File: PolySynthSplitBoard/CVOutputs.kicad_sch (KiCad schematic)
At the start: 121 parts, among them U301 DAC7578xPW, U302 TL074, U303 TL072, U304 TL074, U305 TL072, U306 TMUX4051, U307 TL074, U308 TMUX4051, U309 TL072, U310 TL074, U311 TL072, U312 TL074, U313 TMUX4051, U314 TMUX4051, U315 TL074, U316 TL074, U317 TL074, U318 TL072, U319 TL072, U320 TL072, U321 TMUX4051, U322 TMUX4051, U323 TMUX4051

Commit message: lower board
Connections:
- net FOLD_DAC: now also U301.11 (VOUTF); no longer U301.6 (VOUTE)
- net PWM1_DAC: now also U301.6 (VOUTE); no longer U301.5 (VOUTC)
- net PWM2_DAC: now also U301.5 (VOUTC); no longer U301.12 (VOUTD)
- net VCA_DAC: now also U301.12 (VOUTD); no longer U301.11 (VOUTF)
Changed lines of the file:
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@@
 	(wire
 		(pts
-			(xy 76.2 71.628) (xy 79.756 71.628)
+			(xy 76.2 71.628) (xy 80.518 71.628)
 		)
 		(stroke
@@
 	(wire
 		(pts
+			(xy 76.2 69.088) (xy 80.518 69.088)
+		)
+		(stroke
+			(width 0)
+			(type default)
+		)
+	)
+	(wire
+		(pts
 			(xy 432.816 125.984) (xy 432.816 117.094)
 		)
@@
 	(wire
 		(pts
-			(xy 76.2 69.088) (xy 79.756 69.088)
-		)
-		(stroke
-			(width 0)
-			(type default)
-		)
-	)
-	(wire
-		(pts
 			(xy 495.808 176.276) (xy 500.888 176.276)
 		)
@@
 	(global_label "PWM2_DAC"
 		(shape output)
-		(at 79.756 71.628 0)
+		(at 80.518 69.088 0)
 		(fields_autoplaced yes)
 		(effects
@@
 		)
 		(property "Intersheetrefs" "${INTERSHEET_REFS}"
-			(at 92.7197 71.628 0)
+			(at 93.4817 69.088 0)
 			(effects
 				(font
@@
 	(global_label "VCA_DAC"
 		(shape output)
-		(at 80.518 76.708 0)
+		(at 80.518 71.628 0)
 		(fields_autoplaced yes)
 		(effects
@@
 		)
 		(property "Intersheetrefs" "${INTERSHEET_REFS}"
-			(at 91.5466 76.708 0)
+			(at 91.5466 71.628 0)
 			(effects
 				(font
@@
 	(global_label "PWM1_DAC"
 		(shape output)
-		(at 79.756 69.088 0)
+		(at 80.518 74.168 0)
 		(fields_autoplaced yes)
 		(effects
@@
 		)
 		(property "Intersheetrefs" "${INTERSHEET_REFS}"
-			(at 92.7197 69.088 0)
+			(at 93.4817 74.168 0)
 			(effects
 				(font
@@
 	(global_label "FOLD_DAC"
 		(shape output)
-		(at 80.518 74.168 0)
+		(at 80.518 76.708 0)
 		(fields_autoplaced yes)
 		(effects
@@
 		)
 		(property "Intersheetrefs" "${INTERSHEET_REFS}"
-			(at 92.8166 74.168 0)
+			(at 92.8166 76.708 0)
 			(effects
 				(font

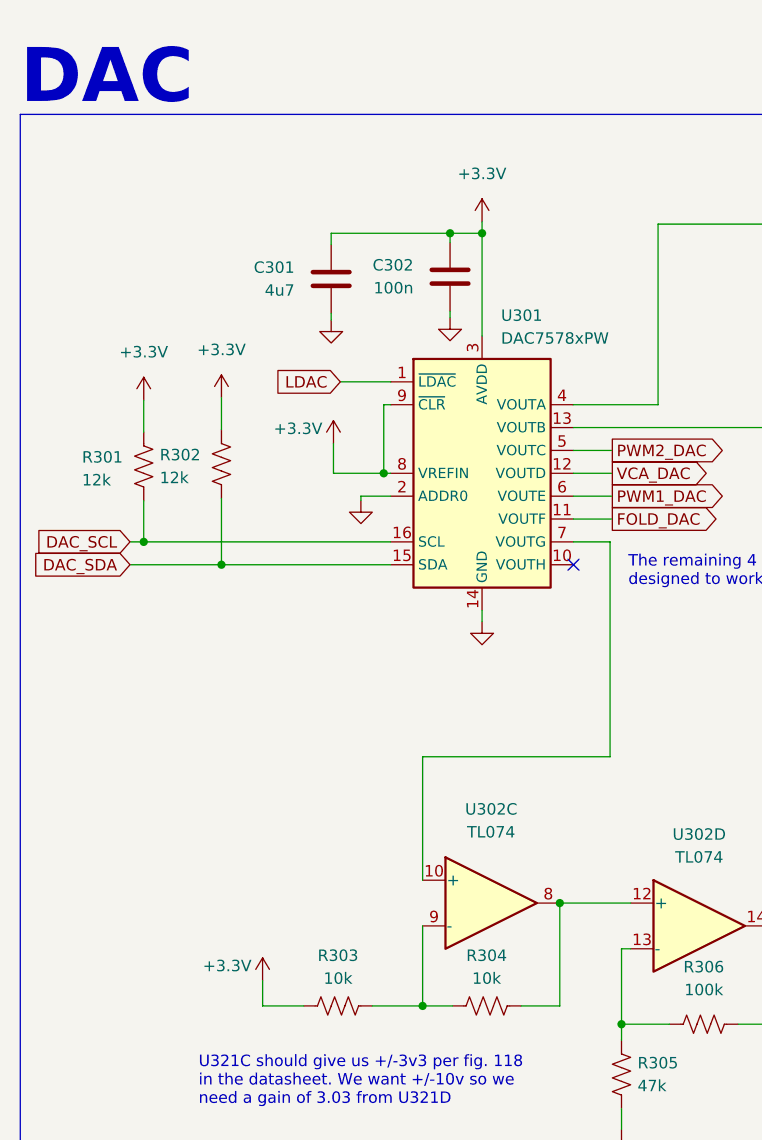
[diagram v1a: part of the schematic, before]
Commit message: removed copper pour
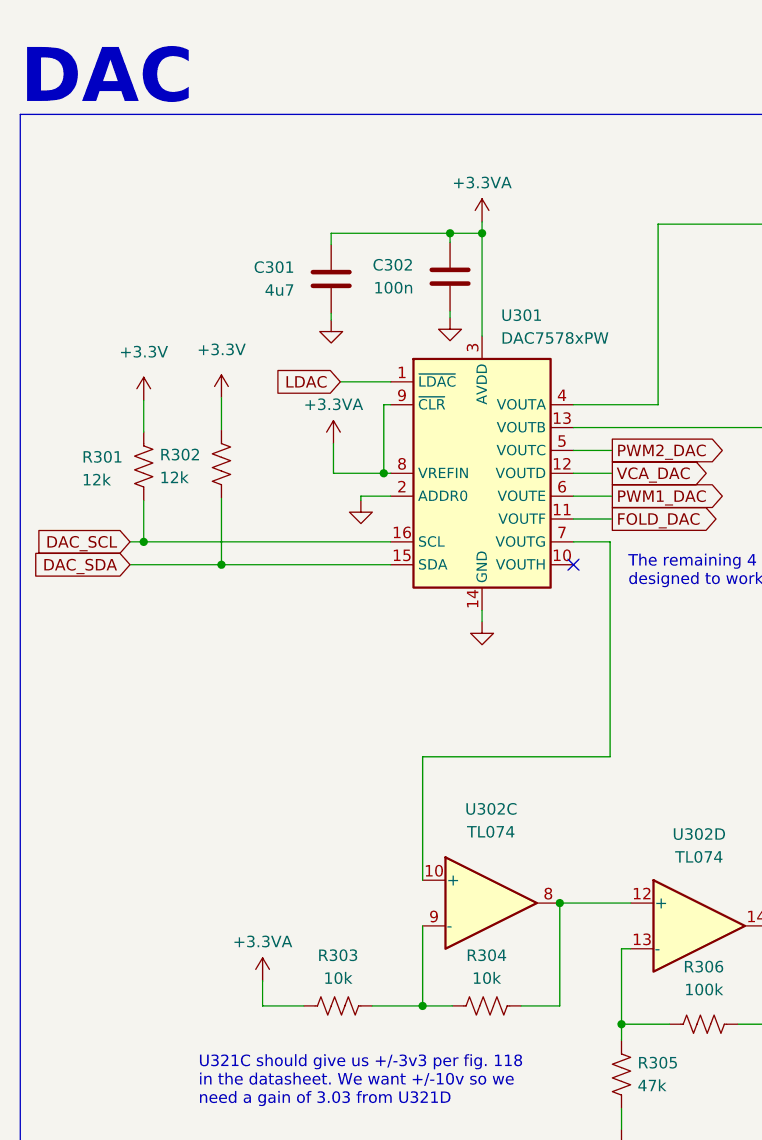
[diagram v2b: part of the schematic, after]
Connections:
- net +3.3V: no longer C301.1, C302.1, R303.1, U301.3 (AVDD), U301.8 (VREFIN), U301.9 (~{CLR})
- new net +3.3VA: C301.1, C302.1, R303.1, U301.3 (AVDD), U301.8 (VREFIN), U301.9 (~{CLR})
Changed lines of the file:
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@@
 	)
 	(symbol
-		(lib_name "+3.3V_1")
-		(lib_id "power:+3.3V")
-		(at 66.04 43.688 0)
-		(unit 1)
-		(exclude_from_sim no)
-		(in_bom yes)
-		(on_board yes)
-		(dnp no)
-		(fields_autoplaced yes)
-		(property "Reference" "#PWR0308"
-			(at 66.04 47.498 0)
-			(effects
-				(font
-					(size 1.27 1.27)
-				)
-				(hide yes)
-			)
-		)
-		(property "Value" "+3.3V"
-			(at 66.04 38.354 0)
-			(effects
-				(font
-					(size 1.27 1.27)
-				)
-			)
-		)
-		(property "Footprint" ""
-			(at 66.04 43.688 0)
-			(effects
-				(font
-					(size 1.27 1.27)
-				)
-				(hide yes)
-			)
-		)
-		(property "Datasheet" ""
-			(at 66.04 43.688 0)
-			(effects
-				(font
-					(size 1.27 1.27)
-				)
-				(hide yes)
-			)
-		)
-		(property "Description" "Power symbol creates a global label with name \"+3.3V\""
-			(at 66.04 43.688 0)
-			(effects
-				(font
-					(size 1.27 1.27)
-				)
-				(hide yes)
-			)
-		)
-		(pin "1"
-		)
-		(instances
-			(project "PolySynthSplitBoard"
-				(path "/22649217-9810-470f-bc7b-6f743ad2b90e/3d9ecb3b-9556-42d6-955a-a32d9efd5d3a/21390c27-a24b-4358-ba76-7238fda06c1e"
-					(reference "#PWR0308")
-					(unit 1)
-				)
-			)
-		)
-	)
-	(symbol
 		(lib_id "Device:C")
 		(at 469.9 199.644 270)
@@
 	)
 	(symbol
-		(lib_id "power:+3.3V")
-		(at 41.656 128.016 0)
-		(unit 1)
-		(exclude_from_sim no)
-		(in_bom yes)
-		(on_board yes)
-		(dnp no)
-		(property "Reference" "#PWR0303"
-			(at 41.656 131.826 0)
-			(effects
-				(font
-					(size 1.27 1.27)
-				)
-				(hide yes)
-			)
-		)
-		(property "Value" "+3.3V"
-			(at 37.719 126.365 0)
-			(effects
-				(font
-					(size 1.27 1.27)
-				)
-			)
-		)
-		(property "Footprint" ""
-			(at 41.656 128.016 0)
-			(effects
-				(font
-					(size 1.27 1.27)
-				)
-				(hide yes)
-			)
-		)
-		(property "Datasheet" ""
-			(at 41.656 128.016 0)
-			(effects
-				(font
-					(size 1.27 1.27)
-				)
-				(hide yes)
-			)
-		)
-		(property "Description" ""
-			(at 41.656 128.016 0)
-			(effects
-				(font
-					(size 1.27 1.27)
-				)
-				(hide yes)
-			)
-		)
-		(pin "1"
-		)
-		(instances
-			(project "PolySynthSplitBoard"
-				(path "/22649217-9810-470f-bc7b-6f743ad2b90e/3d9ecb3b-9556-42d6-955a-a32d9efd5d3a/21390c27-a24b-4358-ba76-7238fda06c1e"
-					(reference "#PWR0303")
-					(unit 1)
-				)
-			)
-		)
-	)
-	(symbol
 		(lib_id "Device:C")
 		(at 227.33 107.188 0)
@@
 	)
 	(symbol
-		(lib_id "power:+3.3V")
-		(at 49.53 68.326 0)
-		(unit 1)
-		(exclude_from_sim no)
-		(in_bom yes)
-		(on_board yes)
-		(dnp no)
-		(property "Reference" "#PWR0305"
-			(at 49.53 72.136 0)
-			(effects
-				(font
-					(size 1.27 1.27)
-				)
-				(hide yes)
-			)
-		)
-		(property "Value" "+3.3V"
-			(at 45.593 66.675 0)
-			(effects
-				(font
-					(size 1.27 1.27)
-				)
-			)
-		)
-		(property "Footprint" ""
-			(at 49.53 68.326 0)
-			(effects
-				(font
-					(size 1.27 1.27)
-				)
-				(hide yes)
-			)
-		)
-		(property "Datasheet" ""
-			(at 49.53 68.326 0)
-			(effects
-				(font
-					(size 1.27 1.27)
-				)
-				(hide yes)
-			)
-		)
-		(property "Description" ""
-			(at 49.53 68.326 0)
-			(effects
-				(font
-					(size 1.27 1.27)
-				)
-				(hide yes)
-			)
-		)
-		(pin "1"
-		)
-		(instances
-			(project "PolySynthSplitBoard"
-				(path "/22649217-9810-470f-bc7b-6f743ad2b90e/3d9ecb3b-9556-42d6-955a-a32d9efd5d3a/21390c27-a24b-4358-ba76-7238fda06c1e"
-					(reference "#PWR0305")
-					(unit 1)
-				)
-			)
-		)
-	)
-	(symbol
 		(lib_id "Amplifier_Operational:TL072")
 		(at 477.012 232.918 0)
@@
 	)
 	(symbol
+		(lib_id "power:+3.3VA")
+		(at 66.04 43.688 0)
+		(unit 1)
+		(exclude_from_sim no)
+		(in_bom yes)
+		(on_board yes)
+		(dnp no)
+		(fields_autoplaced yes)
+		(property "Reference" "#PWR0308"
+			(at 66.04 47.498 0)
+			(effects
+				(font
+					(size 1.27 1.27)
+				)
+				(hide yes)
+			)
+		)
+		(property "Value" "+3.3VA"
+			(at 66.04 39.37 0)
+			(effects
+				(font
+					(size 1.27 1.27)
+				)
+			)
+		)
+		(property "Footprint" ""
+			(at 66.04 43.688 0)
+			(effects
+				(font
+					(size 1.27 1.27)
+				)
+				(hide yes)
+			)
+		)
+		(property "Datasheet" ""
+			(at 66.04 43.688 0)
+			(effects
+				(font
+					(size 1.27 1.27)
+				)
+				(hide yes)
+			)
+		)
+		(property "Description" "Power symbol creates a global label with name \"+3.3VA\""
+			(at 66.04 43.688 0)
+			(effects
+				(font
+					(size 1.27 1.27)
+				)
+				(hide yes)
+			)
+		)
+		(pin "1"
+		)
+		(instances
+			(project ""
+				(path "/22649217-9810-470f-bc7b-6f743ad2b90e/3d9ecb3b-9556-42d6-955a-a32d9efd5d3a/21390c27-a24b-4358-ba76-7238fda06c1e"
+					(reference "#PWR0308")
+					(unit 1)
+				)
+			)
+		)
+	)
+	(symbol
 		(lib_id "Device:C")
 		(at 483.108 274.574 270)
@@
 	)
 	(symbol
+		(lib_id "power:+3.3VA")
+		(at 49.53 68.326 0)
+		(unit 1)
+		(exclude_from_sim no)
+		(in_bom yes)
+		(on_board yes)
+		(dnp no)
+		(fields_autoplaced yes)
+		(property "Reference" "#PWR0305"
+			(at 49.53 72.136 0)
+			(effects
+				(font
+					(size 1.27 1.27)
+				)
+				(hide yes)
+			)
+		)
+		(property "Value" "+3.3VA"
+			(at 49.53 64.008 0)
+			(effects
+				(font
+					(size 1.27 1.27)
+				)
+			)
+		)
+		(property "Footprint" ""
+			(at 49.53 68.326 0)
+			(effects
+				(font
+					(size 1.27 1.27)
+				)
+				(hide yes)
+			)
+		)
+		(property "Datasheet" ""
+			(at 49.53 68.326 0)
+			(effects
+				(font
+					(size 1.27 1.27)
+				)
+				(hide yes)
+			)
+		)
+		(property "Description" "Power symbol creates a global label with name \"+3.3VA\""
+			(at 49.53 68.326 0)
+			(effects
+				(font
+					(size 1.27 1.27)
+				)
+				(hide yes)
+			)
+		)
+		(pin "1"
+		)
+		(instances
+			(project "PolySynthSplitBoard"
+				(path "/22649217-9810-470f-bc7b-6f743ad2b90e/3d9ecb3b-9556-42d6-955a-a32d9efd5d3a/21390c27-a24b-4358-ba76-7238fda06c1e"
+					(reference "#PWR0305")
+					(unit 1)
+				)
+			)
+		)
+	)
+	(symbol
 		(lib_id "Device:C")
 		(at 407.924 69.088 0)
@@
 					(unit 1)
 				)
+			)
+		)
+	)
+	(symbol
+		(lib_id "power:+3.3VA")
+		(at 41.656 128.016 0)
+		(unit 1)
+		(exclude_from_sim no)
+		(in_bom yes)
+		(on_board yes)
+		(dnp no)
+		(fields_autoplaced yes)
+		(property "Reference" "#PWR0303"
+			(at 41.656 131.826 0)
+			(effects
+				(font
+					(size 1.27 1.27)
+				)
+				(hide yes)
+			)
+		)
+		(property "Value" "+3.3VA"
+			(at 41.656 123.698 0)
+			(effects
+				(font
+					(size 1.27 1.27)
+				)
+			)
+		)
+		(property "Footprint" ""
+			(at 41.656 128.016 0)
+			(effects
+				(font
+					(size 1.27 1.27)
+				)
+				(hide yes)
+			)
+		)
+		(property "Datasheet" ""
+			(at 41.656 128.016 0)
+			(effects
+				(font
+					(size 1.27 1.27)
+				)
+				(hide yes)
+			)
+		)
+		(property "Description" "Power symbol creates a global label with name \"+3.3VA\""
+			(at 41.656 128.016 0)
+			(effects
+				(font
+					(size 1.27 1.27)
+				)
+				(hide yes)
+			)
+		)
+		(pin "1"
+		)
+		(instances
+			(project "PolySynthSplitBoard"
+				(path "/22649217-9810-470f-bc7b-6f743ad2b90e/3d9ecb3b-9556-42d6-955a-a32d9efd5d3a/21390c27-a24b-4358-ba76-7238fda06c1e"
+					(reference "#PWR0303")
+					(unit 1)
+				)

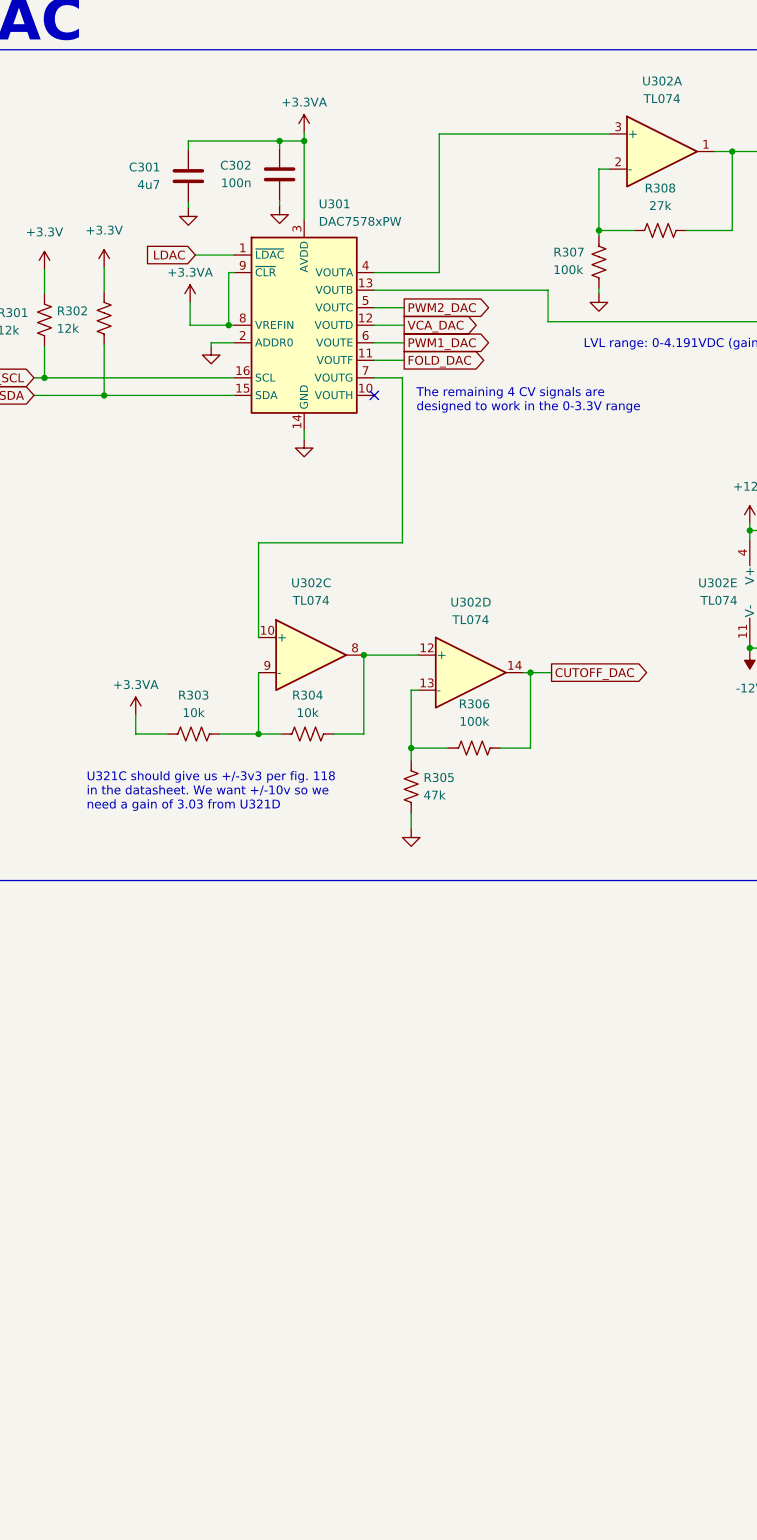
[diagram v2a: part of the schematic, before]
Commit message: more test points
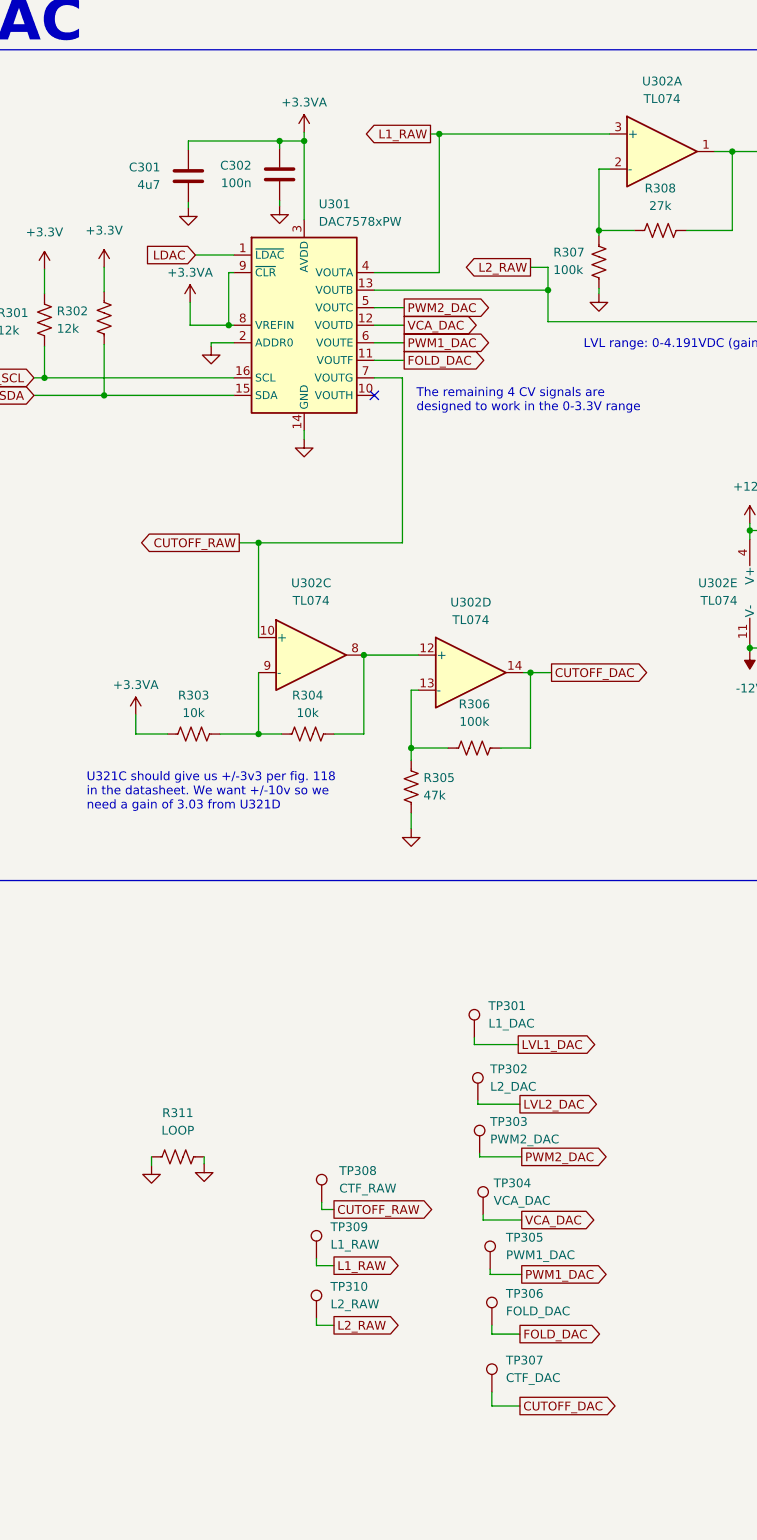
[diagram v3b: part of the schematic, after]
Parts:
- added R311: LOOP, Resistor_THT:R_Axial_DIN0204_L3.6mm_D1.6mm_P5.08mm_Horizontal, symbol Device:R_US
- added TP301: L1_DAC, TestPoint:TestPoint_THTPad_D1.0mm_Drill0.5mm_VAL, symbol Connector:TestPoint
- added TP302: L2_DAC, TestPoint:TestPoint_THTPad_D1.0mm_Drill0.5mm_VAL, symbol Connector:TestPoint
- added TP303: PWM2_DAC, TestPoint:TestPoint_THTPad_D1.0mm_Drill0.5mm_VAL, symbol Connector:TestPoint
- added TP304: VCA_DAC, TestPoint:TestPoint_THTPad_D1.0mm_Drill0.5mm_VAL, symbol Connector:TestPoint
- added TP305: PWM1_DAC, TestPoint:TestPoint_THTPad_D1.0mm_Drill0.5mm_VAL, symbol Connector:TestPoint
- added TP306: FOLD_DAC, TestPoint:TestPoint_THTPad_D1.0mm_Drill0.5mm_VAL, symbol Connector:TestPoint
- added TP307: CTF_DAC, TestPoint:TestPoint_THTPad_D1.0mm_Drill0.5mm_VAL, symbol Connector:TestPoint
- added TP308: CTF_RAW, TestPoint:TestPoint_THTPad_D1.0mm_Drill0.5mm_VAL, symbol Connector:TestPoint
- added TP309: L1_RAW, TestPoint:TestPoint_THTPad_D1.0mm_Drill0.5mm_VAL, symbol Connector:TestPoint
- added TP310: L2_RAW, TestPoint:TestPoint_THTPad_D1.0mm_Drill0.5mm_VAL, symbol Connector:TestPoint
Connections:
- net CUTOFF_DAC: now also TP307.1
- net FOLD_DAC: now also TP306.1
- net GND: now also R311.1, R311.2
- net LVL1_DAC: now also TP301.1
- net LVL2_DAC: now also TP302.1
- net PWM1_DAC: now also TP305.1
- net PWM2_DAC: now also TP303.1
- net VCA_DAC: now also TP304.1
- net CUTOFF_RAW: now reaches U301.7 (VOUTG), U302.10 (+)
- net CUTOFF_RAW: now also TP308.1
- net L2_RAW: now reaches U301.13 (VOUTB), U302.5 (+)
- net L2_RAW: now also TP310.1
- net L1_RAW: now reaches U301.4 (VOUTA), U302.3 (+)
- net L1_RAW: now also TP309.1

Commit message: mod matrix logic stuff
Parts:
- TP301: value L1_DAC -> TestPoint; now left out of the parts list
- TP302: value L2_DAC -> TestPoint; now left out of the parts list
- TP303: value PWM2_DAC -> TestPoint; now left out of the parts list
- TP304: value VCA_DAC -> TestPoint; now left out of the parts list
- TP305: value PWM1_DAC -> TestPoint; now left out of the parts list
- TP306: value FOLD_DAC -> TestPoint; now left out of the parts list
- TP307: value CTF_DAC -> TestPoint; now left out of the parts list
- TP308: value CTF_RAW -> TestPoint; now left out of the parts list
- TP309: value L1_RAW -> TestPoint; now left out of the parts list
- TP310: value L2_RAW -> TestPoint; now left out of the parts list
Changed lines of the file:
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@@
 		(unit 1)
 		(exclude_from_sim no)
-		(in_bom yes)
+		(in_bom no)
 		(on_board yes)
 		(dnp no)
@@
 			)
 		)
-		(property "Value" "FOLD_DAC"
+		(property "Value" "TestPoint"
 			(at 95.25 214.3759 0)
 			(effects
@@
 		(unit 1)
 		(exclude_from_sim no)
-		(in_bom yes)
+		(in_bom no)
 		(on_board yes)
 		(dnp no)
@@
 			)
 		)
-		(property "Value" "L1_DAC"
+		(property "Value" "TestPoint"
 			(at 92.71 172.7199 0)
 			(effects
@@
 		(unit 1)
 		(exclude_from_sim no)
-		(in_bom yes)
+		(in_bom no)
 		(on_board yes)
 		(dnp no)
@@
 			)
 		)
-		(property "Value" "L2_RAW"
+		(property "Value" "TestPoint"
 			(at 69.85 213.3599 0)
 			(effects
@@
 		(unit 1)
 		(exclude_from_sim no)
-		(in_bom yes)
+		(in_bom no)
 		(on_board yes)
 		(dnp no)
@@
 			)
 		)
-		(property "Value" "CTF_RAW"
+		(property "Value" "TestPoint"
 			(at 71.12 196.5959 0)
 			(effects
@@
 		(unit 1)
 		(exclude_from_sim no)
-		(in_bom yes)
+		(in_bom no)
 		(on_board yes)
 		(dnp no)
@@
 			)
 		)
-		(property "Value" "CTF_DAC"
+		(property "Value" "TestPoint"
 			(at 95.25 224.0279 0)
 			(effects
@@
 		(unit 1)
 		(exclude_from_sim no)
-		(in_bom yes)
+		(in_bom no)
 		(on_board yes)
 		(dnp no)
 		(fields_autoplaced yes)
 		(property "Reference" "TP302"
-			(at 92.964 179.3239 0)
+			(at 92.71 179.3239 0)
 			(effects
 				(font
@@
 			)
 		)
-		(property "Value" "L2_DAC"
-			(at 92.964 181.8639 0)
+		(property "Value" "TestPoint"
+			(at 92.71 181.8639 0)
 			(effects
 				(font
@@
 		(unit 1)
 		(exclude_from_sim no)
-		(in_bom yes)
+		(in_bom no)
 		(on_board yes)
 		(dnp no)
 		(fields_autoplaced yes)
 		(property "Reference" "TP304"
-			(at 93.472 195.8339 0)
+			(at 93.98 195.8339 0)
 			(effects
 				(font
@@
 			)
 		)
-		(property "Value" "VCA_DAC"
-			(at 93.472 198.3739 0)
+		(property "Value" "TestPoint"
+			(at 93.98 198.3739 0)
 			(effects
 				(font
@@
 		(unit 1)
 		(exclude_from_sim no)
-		(in_bom yes)
+		(in_bom no)
 		(on_board yes)
 		(dnp no)
 		(fields_autoplaced yes)
 		(property "Reference" "TP303"
-			(at 92.964 186.9439 0)
+			(at 93.98 186.9439 0)
 			(effects
 				(font
@@
 			)
 		)
-		(property "Value" "PWM2_DAC"
-			(at 92.964 189.4839 0)
+		(property "Value" "TestPoint"
+			(at 93.98 189.4839 0)
 			(effects
 				(font
@@
 		(unit 1)
 		(exclude_from_sim no)
-		(in_bom yes)
+		(in_bom no)
 		(on_board yes)
 		(dnp no)
@@
 			)
 		)
-		(property "Value" "L1_RAW"
+		(property "Value" "TestPoint"
 			(at 69.85 204.7239 0)
 			(effects
@@
 		(unit 1)
 		(exclude_from_sim no)
-		(in_bom yes)
+		(in_bom no)
 		(on_board yes)
 		(dnp no)
@@
 			)
 		)
-		(property "Value" "PWM1_DAC"
+		(property "Value" "TestPoint"
 			(at 95.25 206.2479 0)
 			(effects
